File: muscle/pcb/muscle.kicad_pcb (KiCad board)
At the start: 4 copper layers, 119.5 x 50 mm, 134 parts, among them J1 B4B-XH-2(LF)(SN), J10 USB4115-03-C, J2 WAFER-SH1.0-3PWB, J3 XT30UPB-M, J4 WAFER-SH1.0-3PWB, J5 B4B-XH-2(LF)(SN), J8 B2B-XH-A(LF)(SN), Q2 WSD4070DN33, Q3 WSD4070DN33, Q4 WSD4070DN33, Q5 BSS138W, Q6 WSD4070DN33, Q8 WSD4070DN33, SW1 GT-TC041B-H036-L1N, SW2 GT-TC041B-H036-L1N, U1 TMC2209-LA, U12 TPD2EUSB30A, U13 TLV75733PDBV, U14 DRV8701P, U17 TPS16630PWP, U2 TMC2209-LA, U3 RP2350A, U4 LM5050-1, U5 TPS2061CDBV, U6 XT25F128FWOIGT-W, U8 TUSB320LI, U9 TPS62933, Y1 ABM8-272-T3

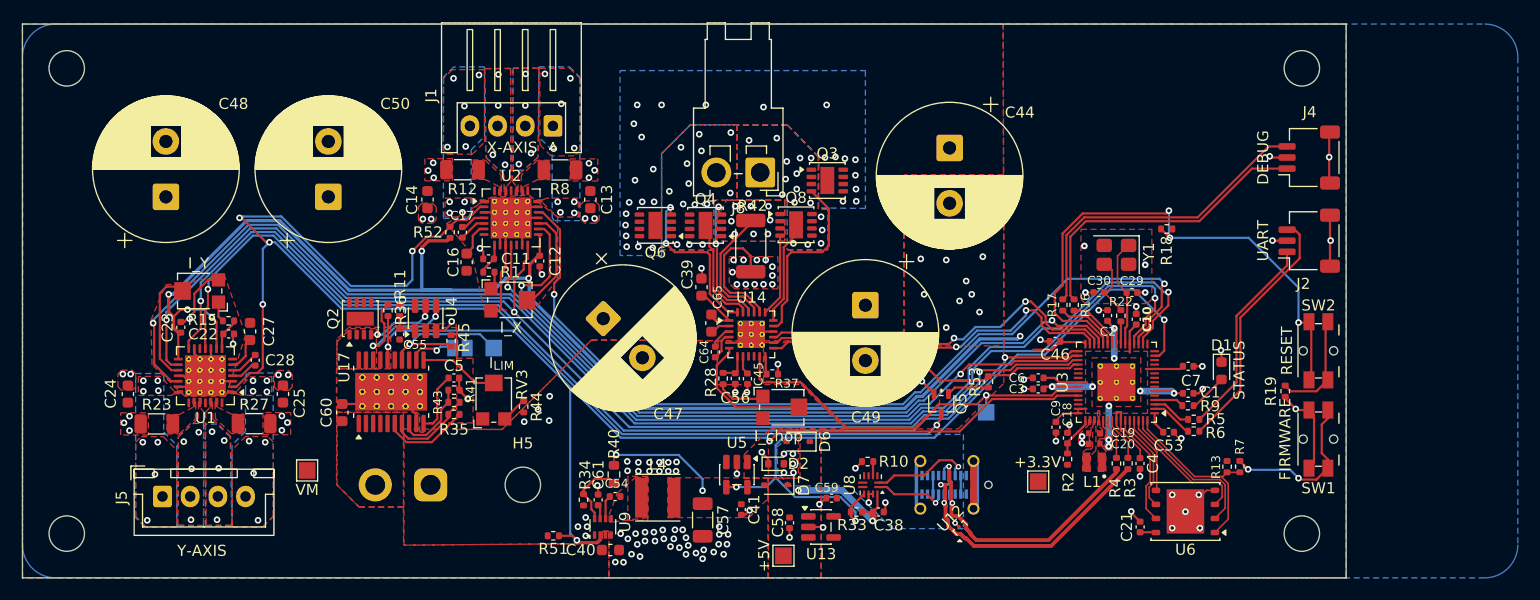
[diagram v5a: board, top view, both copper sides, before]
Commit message: muscle: switch to DRV8734A stepper drivers
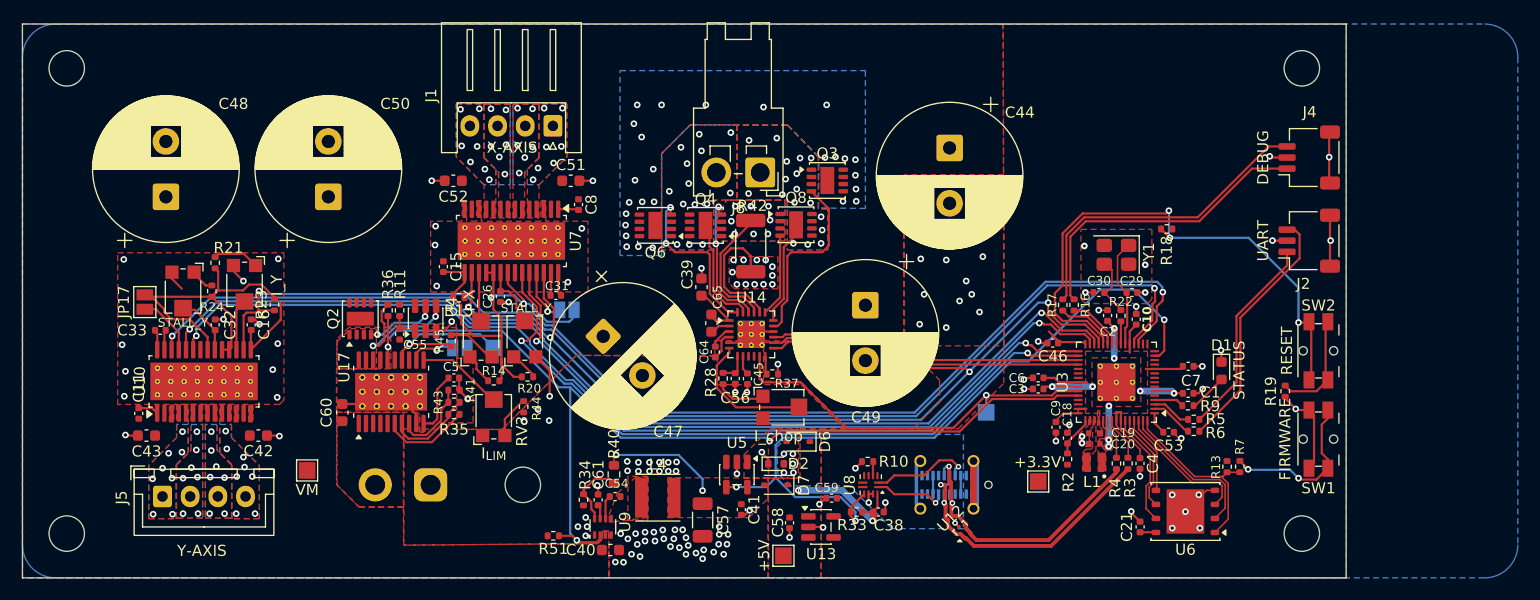
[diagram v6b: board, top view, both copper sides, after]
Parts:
- removed C12, C23: 1u, Capacitor_SMD:C_0402_1005Metric
- removed C13, C14, C24, C25: 1u, Capacitor_SMD:C_0603_1608Metric
- removed C17, C28: 22n, Capacitor_SMD:C_0402_1005Metric
- removed C22: 10u, Capacitor_SMD:C_0402_1005Metric
- removed C27: 100n, Capacitor_SMD:C_0603_1608Metric
- removed Q5: BSS138W, Package_TO_SOT_SMD:SOT-323_SC-70
- removed R1, R52: 10k, Resistor_SMD:R_0402_1005Metric
- removed R12, R27, R8: 120m,1%,1W, Resistor_SMD:R_1206_3216Metric
- removed R53: 1k, Resistor_SMD:R_0402_1005Metric
- removed RV6: I_X, Potentiometer_SMD:Potentiometer_Bourns_TC33X_Vertical
- removed RV7: I_Y, Potentiometer_SMD:Potentiometer_Bourns_TC33X_Vertical
- removed U1, U2: TMC2209-LA, Package_DFN_QFN:VQFN-28-1EP_5x5mm_P0.5mm_EP3.7x3.7mm_ThermalVias
- added C15: 10u, Capacitor_SMD:C_0402_1005Metric, F.Cu at (101.0, 97.9)
- added C26: 1n, Capacitor_SMD:C_0402_1005Metric, F.Cu at (106.2, 100.6)
- added C31: 22n, Capacitor_SMD:C_0402_1005Metric, F.Cu at (111.2, 100.5)
- added C32: 1n, Capacitor_SMD:C_0402_1005Metric, F.Cu at (80.4, 103.2)
- added C33: 22n, Capacitor_SMD:C_0402_1005Metric, F.Cu at (75.5, 103.7)
- added C42: 10u, Capacitor_SMD:C_0603_1608Metric, F.Cu at (84.3, 113.2)
- added C43: 10u, Capacitor_SMD:C_0603_1608Metric, F.Cu at (74.2, 113.2)
- added C51: 10u, Capacitor_SMD:C_0603_1608Metric, F.Cu at (112.5, 90.2)
- added C52: 10u, Capacitor_SMD:C_0603_1608Metric, F.Cu at (101.9, 90.2)
- added C8: 220n, Capacitor_SMD:C_0402_1005Metric, F.Cu at (113.2, 92.3)
- added JP16: ~, Jumper:SolderJumper-2_P1.3mm_Open_Pad1.0x1.5mm, B.Cu at (112.2, 101.8)
- added JP17: ~, Jumper:SolderJumper-2_P1.3mm_Open_Pad1.0x1.5mm, F.Cu at (74.0, 101.1)
- added R14: 5.1k, Resistor_SMD:R_0402_1005Metric, F.Cu at (105.5, 108.2)
- added R20: 10k, Resistor_SMD:R_0402_1005Metric, F.Cu at (108.6, 107.8)
- added R21: 5.1k, Resistor_SMD:R_0402_1005Metric, F.Cu at (80.4, 97.5)
- added R24: 10k, Resistor_SMD:R_0402_1005Metric, F.Cu at (80.1, 100.1)
- added RV10: I_Y, Potentiometer_SMD:Potentiometer_Bourns_TC33X_Vertical, F.Cu at (83.0, 99.6)
- added RV11: STALL_Y, Potentiometer_SMD:Potentiometer_Bourns_TC33X_Vertical, F.Cu at (77.5, 100.2)
- added RV8: I_X, Potentiometer_SMD:Potentiometer_Bourns_TC33X_Vertical, F.Cu at (104.4, 104.2)
- added RV9: STALL_X, Potentiometer_SMD:Potentiometer_Bourns_TC33X_Vertical, F.Cu at (108.3, 104.2)
- added U10: DRV8434APWP, Package_SO:TSSOP-28-1EP_4.4x9.7mm_P0.65mm_EP3.4x9.7mm_Mask3.1x4.05mm_ThermalVias, F.Cu at (79.4, 108.3)
- added U7: DRV8434APWP, Package_SO:TSSOP-28-1EP_4.4x9.7mm_P0.65mm_EP3.4x9.7mm_Mask3.1x4.05mm_ThermalVias, F.Cu at (107.1, 95.6)
- C11: value 10u -> 220n
- C16: value 100n -> 10u; footprint Capacitor_SMD:C_0603_1608Metric -> Capacitor_SMD:C_0402_1005Metric
- R23: value 120m,1%,1W -> 10k; footprint Resistor_SMD:R_1206_3216Metric -> Resistor_SMD:R_0402_1005Metric
- moved C11 34.5 mm to (73.5, 111.2), turned to 90 degrees
- moved R15 20.9 mm to (102.4, 100.7)
- moved C16 20.3 mm to (83.7, 103.2), turned to -90 degrees
- moved R23 15.1 mm to (85.8, 101.3), turned to 90 degrees
- moved C47 1.60 mm to (115.4, 104.2)
- moved RV3 1.50 mm to (105.5, 111.3)
- moved C46 0.25 mm to (156.0, 104.8)
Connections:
- C11 pad 1: GND -> VM
- C16 pad 1: VM -> GND
- C16 pad 2: Net-(U2-VCP) -> /Y_DVDD
- J1 pad 1: /X_A2 -> /X_A1
- J1 pad 2: /X_A1 -> /X_A2
- J1 pad 3: /X_B1 -> /X_B2
- J1 pad 4: /X_B2 -> /X_B1
- J5 pad 1: /Y_A2 -> /Y_A1
- J5 pad 2: /Y_A1 -> /Y_A2
- J5 pad 3: /Y_B1 -> /Y_B2
- J5 pad 4: /Y_B2 -> /Y_B1
- R15 pad 1: Net-(U1-5VOUT) -> /X_DIAG
- R15 pad 2: Net-(R15-Pad2) -> /X_DVDD
- R23 pad 1: /Y_BRA -> /Y_DIAG
- R23 pad 2: GND -> /Y_DVDD
- U3 pad 17: /Y_DIR -> unconnected-(U3-GPIO13-Pad17)
- U3 pad 18: /X_DIR -> /Y_DIAG
- U3 pad 19: /Y_STEP -> /X_DIAG
- U3 pad 27: /X_STEP -> /DRV_EN
- U3 pad 28: /S_IN1 -> /Y_DIR
- U3 pad 29: /S_IN2 -> /X_DIR
- U3 pad 31: /Y_DIAG -> /Y_STEP
- U3 pad 32: /X_DIAG -> /X_STEP
- U3 pad 33: /STEP_UART -> /S_IN1
- U3 pad 34: /DRV_EN -> /S_IN2
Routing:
- net +3V3: track 147.7 -> 27.7 mm, vias 6 -> 0
- net /~{DRV_EN}: track 116.8 -> 0.00 mm, vias 5 -> 0
- net /STEP_UART: track 104.4 -> 0.00 mm, vias 3 -> 0
- net /DRV_EN: track 33.2 -> 123.1 mm, vias 0 -> 4
- net /Y_DVDD: track 0.00 -> 37.5 mm
- net /X_DVDD: track 0.00 -> 37.2 mm, vias 0 -> 2
- net /Y_DIR: track 121.2 -> 94.9 mm
- net /Y_STEP: track 117.0 -> 91.0 mm
- net /X_DIAG: track 62.6 -> 81.0 mm
- net /X_DIR: track 80.3 -> 64.8 mm
- net GND: track 119.4 -> 105.7 mm, vias 152 -> 148
- net Net-(U1-VREF): track 9.90 -> 0.00 mm
- net Net-(U2-VREF): track 8.64 -> 0.00 mm
- net /Y_DIAG: track 97.0 -> 105.1 mm
- net Net-(JP17-B): track 0.00 -> 5.51 mm
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- removed copper zone on F.Cu, net /X_BRA
- removed copper zone on F.Cu, net /X_BRB
- removed copper zone on F.Cu, net /Y_BRA
- removed copper zone on F.Cu, net /Y_BRB
